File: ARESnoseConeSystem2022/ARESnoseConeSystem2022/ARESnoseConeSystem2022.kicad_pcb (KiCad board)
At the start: 2 copper layers, 125.2 x 66 mm, 39 parts, among them J1 436500200, J2 436500200, J3 BMP390_Headers, J4 ICM20948_Headers, J5 GPS_Headers1, J6 Transmitter_Headers1, J7 Conn_01x08, J8 Transmitter_Headers2, U1 BA05CC0WFP-E2, U2 Teensy4.1

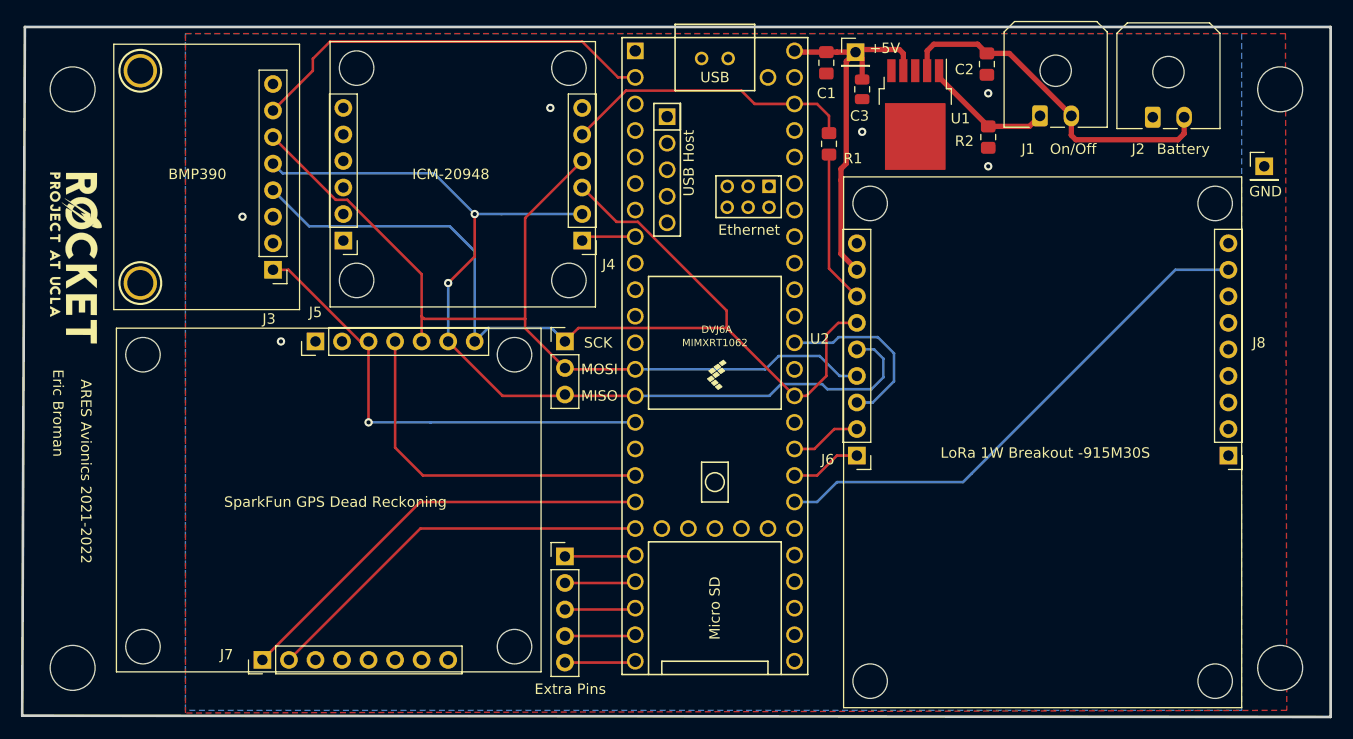
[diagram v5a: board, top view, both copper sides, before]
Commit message: Finalized System V3
Added better radio board access and system power stabiity
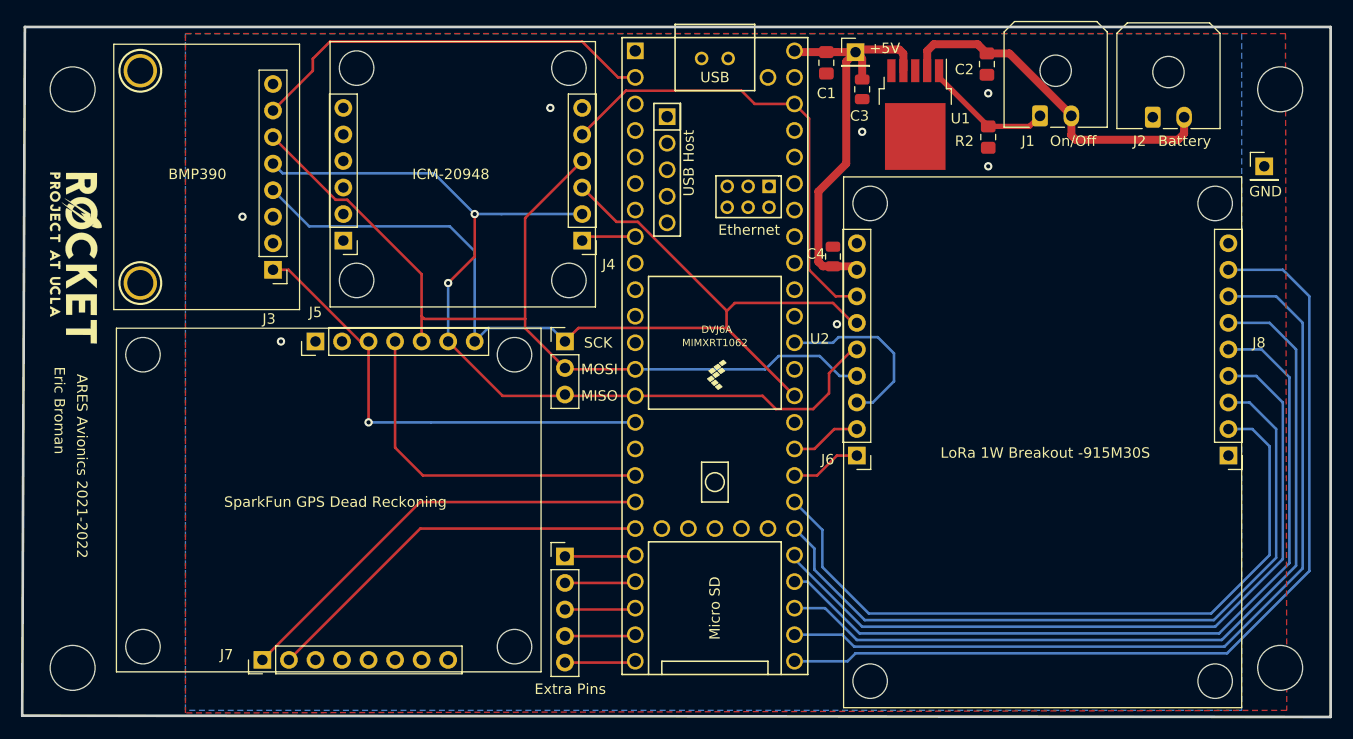
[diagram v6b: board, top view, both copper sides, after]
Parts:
- removed R1: 0 Ohm, Resistor_SMD:R_0805_2012Metric_Pad1.15x1.40mm_HandSolder
- added C4: 10 uF, Capacitor_SMD:C_0805_2012Metric, F.Cu at (124.6, 68.2)
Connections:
- J6 pad 7: Net-(J6-Pad7) -> +3V3
- J8 pad 2: Net-(J8-Pad2) -> /T_D5
- J8 pad 3: Net-(J8-Pad3) -> /T_D4
- J8 pad 4: Net-(J8-Pad4) -> /T_D3
- J8 pad 5: Net-(J8-Pad5) -> /T_D2
- J8 pad 6: Net-(J8-Pad6) -> /T_D1
- J8 pad 7: Net-(J8-Pad7) -> /T_D0
- U2 pad 25: Net-(U2-Pad25) -> /Transmitter_RST
- U2 pad 26: Net-(U2-Pad26) -> /T_D0
- U2 pad 27: Net-(U2-Pad27) -> /T_D1
- U2 pad 28: Net-(U2-Pad28) -> /T_D2
- U2 pad 29: Net-(U2-Pad29) -> /T_D3
- U2 pad 30: Net-(U2-Pad30) -> /T_D4
- U2 pad 31: /Transmitter_RST -> /T_D5
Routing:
- net /T_D0: track 0.00 -> 83.9 mm
- net /T_D1: track 0.00 -> 80.4 mm
- net /T_D2: track 0.00 -> 76.9 mm
- net /T_D3: track 0.00 -> 73.7 mm
- net /T_D4: track 0.00 -> 71.3 mm
- net /T_D5: track 0.00 -> 69.3 mm
- net /Transmitter_RST: track 50.7 -> 87.9 mm
- net +3V3: track 73.3 -> 89.9 mm
- net Net-(J6-Pad7): track 14.7 -> 0.00 mm
- net /MISO: track 94.6 -> 90.2 mm
- net 5V: track 37.3 -> 40.8 mm
- net /SCK: track 96.8 -> 99.2 mm
- net GND: vias 6 -> 7
